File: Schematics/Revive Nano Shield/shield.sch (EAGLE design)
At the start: 24 parts, among them Q3 MOSFET-NCHANNELPTH2

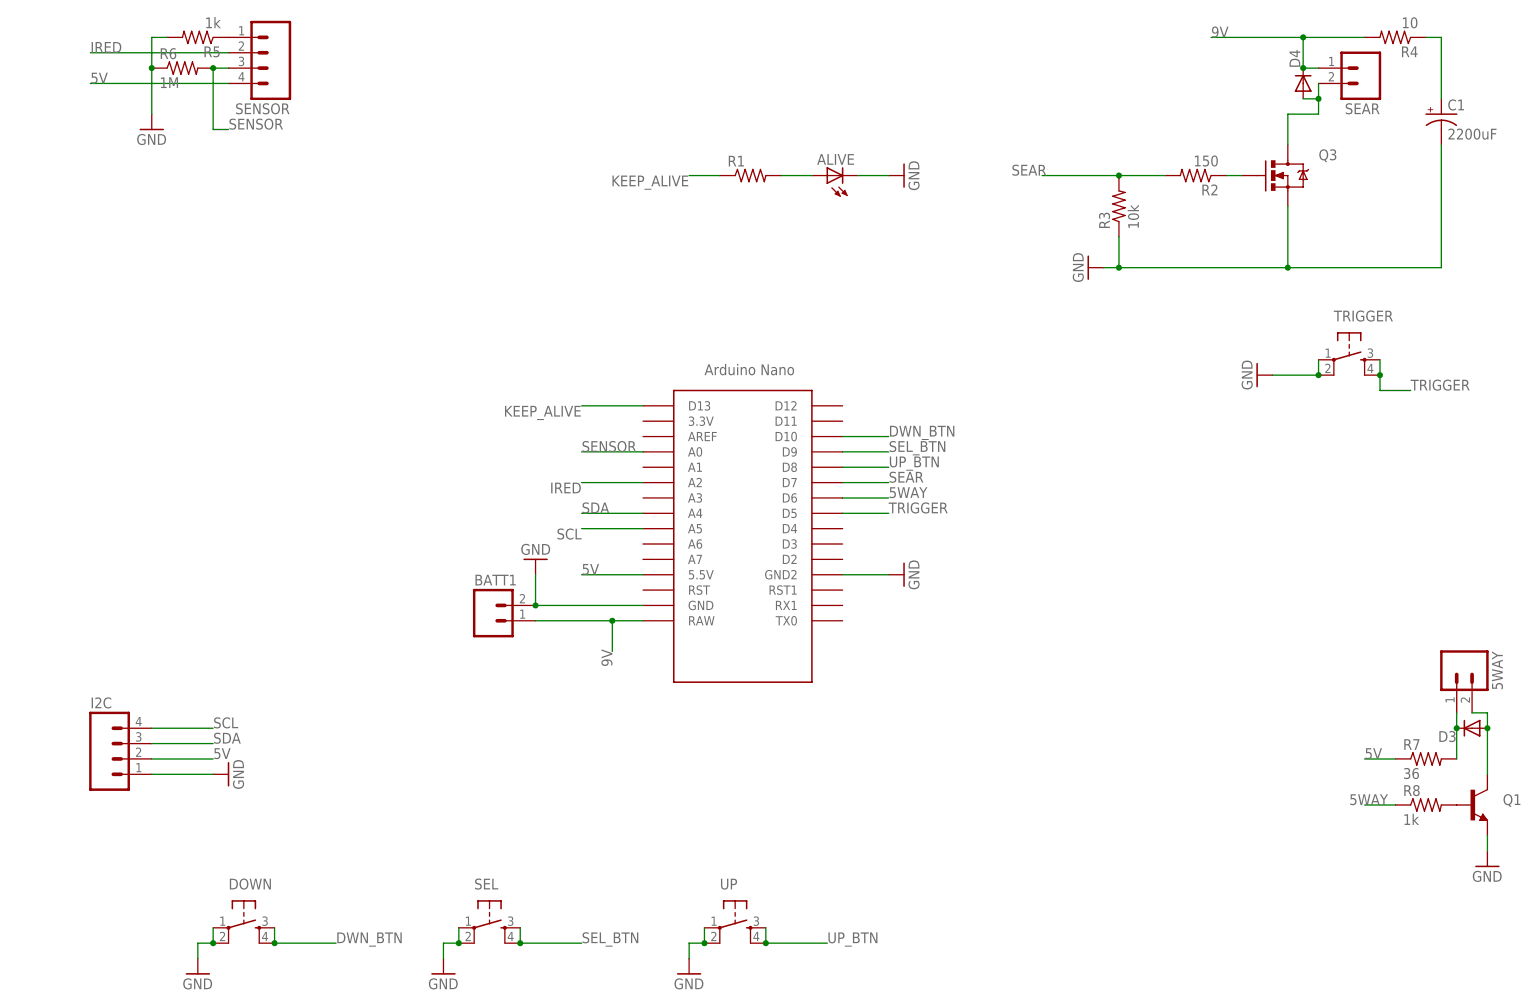
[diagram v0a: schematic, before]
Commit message: Reworks pins to match with new Nano board design
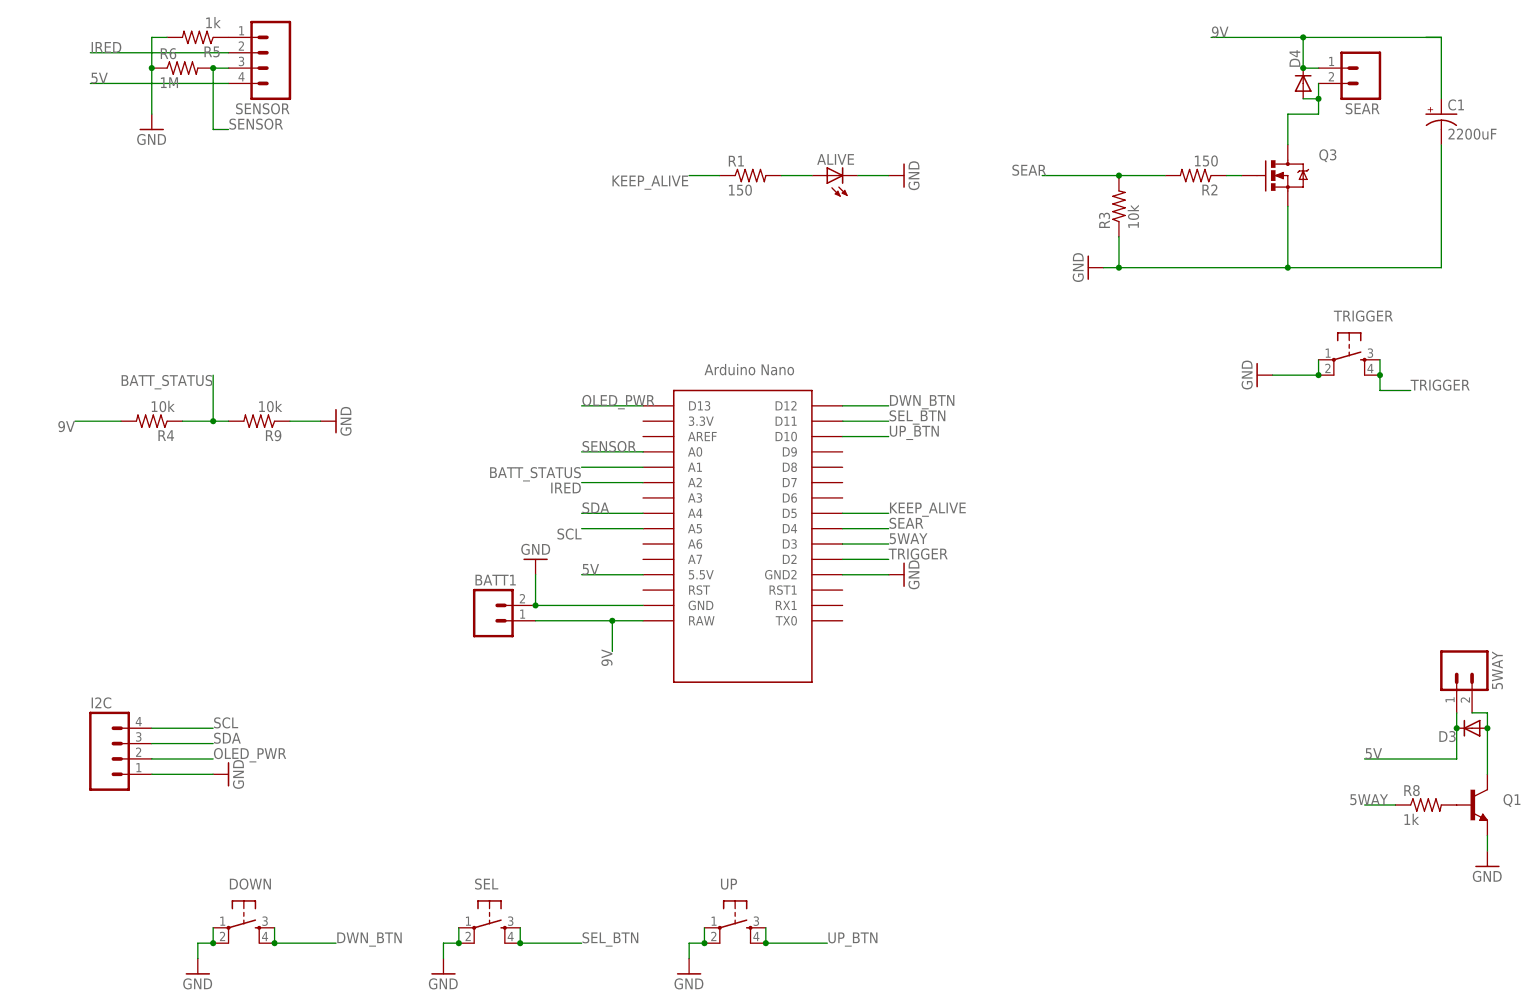
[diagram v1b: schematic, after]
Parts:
- removed R7: 36, SparkFun:RESISTORPTH-1/4W
- added R9: 10k, SparkFun:RESISTORPTH-1/4W
- R1: value (none) -> 150
- R4: value 10 -> 10k
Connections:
- removed net N$4: C1.+, R4.1
- removed net N$5: 5WAY.1, D3.C, R7.2
- new net BATT_STATUS: R4.1, R9.2, U$5.A1
- new net OLED_PWR: I2C.2, U$5.D13
- net 5V: now also 5WAY.1, D3.C; no longer I2C.2, R7.1
- net 5WAY: now also U$5.D3; no longer U$5.D6
- net 9V: now also C1.+
- net DWN_BTN: now also U$5.D12; no longer U$5.D10
- net GND: now also R9.1
- net KEEP_ALIVE: now also U$5.D5; no longer U$5.D13
- net SEAR: now also U$5.D4; no longer U$5.D7
- net SEL_BTN: now also U$5.D11; no longer U$5.D9
- net TRIGGER: now also U$5.D2; no longer U$5.D5
- net UP_BTN: now also U$5.D10; no longer U$5.D8
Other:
- moved on the sheet: R4
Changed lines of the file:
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@@
 <part name="Q3" library="SparkFun" deviceset="MOSFET-NCHANNEL" device="PTH2" value=""/>
 <part name="ALIVE" library="SparkFun" deviceset="LED" device="3MM"/>
-<part name="R1" library="SparkFun" deviceset="RESISTOR" device="PTH-1/4W"/>
+<part name="R1" library="SparkFun" deviceset="RESISTOR" device="PTH-1/4W" value="150"/>
 <part name="GND2" library="SparkFun" deviceset="GND" device=""/>
 <part name="R2" library="SparkFun" deviceset="RESISTOR" device="PTH-1/4W" value="150"/>
-<part name="R4" library="SparkFun" deviceset="RESISTOR" device="PTH-1/4W" value="10"/>
-<part name="R7" library="SparkFun" deviceset="RESISTOR" device="PTH-1/4W" value="36"/>
 <part name="GND5" library="SparkFun" deviceset="GND" device=""/>
 <part name="SEAR" library="SparkFun" deviceset="M02" device="PTH"/>
@@
 <part name="GND7" library="SparkFun" deviceset="GND" device=""/>
 <part name="BATT1" library="SparkFun" deviceset="M02" device="PTH"/>
+<part name="R4" library="SparkFun" deviceset="RESISTOR" device="PTH-1/4W" value="10k"/>
+<part name="R9" library="SparkFun" deviceset="RESISTOR" device="PTH-1/4W" value="10k"/>
+<part name="GND1" library="SparkFun" deviceset="GND" device=""/>
 </parts>
 <sheets>
@@
 <instance part="GND2" gate="1" x="147.32" y="154.94" rot="R90"/>
 <instance part="R2" gate="G$1" x="195.58" y="154.94" rot="R180"/>
-<instance part="R4" gate="G$1" x="228.6" y="177.8" rot="R180"/>
-<instance part="R7" gate="G$1" x="233.68" y="58.42"/>
 <instance part="GND5" gate="1" x="205.74" y="121.92" rot="R270"/>
 <instance part="SEAR" gate="G$1" x="223.52" y="172.72" rot="R180"/>
@@
 <instance part="GND7" gate="1" x="86.36" y="91.44" rot="R180"/>
 <instance part="BATT1" gate="G$1" x="78.74" y="81.28"/>
+<instance part="R4" gate="G$1" x="22.86" y="114.3" rot="R180"/>
+<instance part="R9" gate="G$1" x="40.64" y="114.3" rot="R180"/>
+<instance part="GND1" gate="1" x="53.34" y="114.3" rot="R90"/>
 </instances>
 <busses>
@@
 <wire x1="213.36" y1="172.72" x2="215.9" y2="172.72" width="0.1524" layer="91"/>
 <wire x1="198.12" y1="177.8" x2="213.36" y2="177.8" width="0.1524" layer="91"/>
-<wire x1="213.36" y1="177.8" x2="223.52" y2="177.8" width="0.1524" layer="91"/>
 <wire x1="213.36" y1="172.72" x2="213.36" y2="177.8" width="0.1524" layer="91"/>
-<junction x="213.36" y="177.8"/>
 <label x="198.12" y="177.8" size="1.778" layer="95"/>
 <pinref part="D4" gate="G$1" pin="C"/>
 <junction x="213.36" y="172.72"/>
-<pinref part="R4" gate="G$1" pin="2"/>
 <pinref part="SEAR" gate="G$1" pin="1"/>
+<pinref part="C1" gate="G$1" pin="+"/>
+<wire x1="236.22" y1="167.64" x2="236.22" y2="177.8" width="0.1524" layer="91"/>
+<wire x1="236.22" y1="177.8" x2="213.36" y2="177.8" width="0.1524" layer="91"/>
+<junction x="213.36" y="177.8"/>
 </segment>
 <segment>
@@
 <wire x1="99.06" y1="81.28" x2="99.06" y2="76.2" width="0.1524" layer="91"/>
 <junction x="99.06" y="81.28"/>
+</segment>
+<segment>
+<pinref part="R4" gate="G$1" pin="2"/>
+<wire x1="17.78" y1="114.3" x2="10.16" y2="114.3" width="0.1524" layer="91"/>
+<label x="10.16" y="114.3" size="1.778" layer="95" rot="R180"/>
 </segment>
 </net>
@@
 <wire x1="86.36" y1="83.82" x2="86.36" y2="88.9" width="0.1524" layer="91"/>
 </segment>
+<segment>
+<pinref part="R9" gate="G$1" pin="1"/>
+<pinref part="GND1" gate="1" pin="GND"/>
+<wire x1="50.8" y1="114.3" x2="45.72" y2="114.3" width="0.1524" layer="91"/>
+</segment>
 </net>
 <net name="5V" class="0">
@@
 </segment>
 <segment>
-<pinref part="I2C" gate="G$1" pin="2"/>
-<wire x1="22.86" y1="58.42" x2="33.02" y2="58.42" width="0.1524" layer="91"/>
-<label x="33.02" y="58.42" size="1.778" layer="95"/>
-</segment>
-<segment>
-<pinref part="R7" gate="G$1" pin="1"/>
-<wire x1="228.6" y1="58.42" x2="223.52" y2="58.42" width="0.1524" layer="91"/>
 <label x="223.52" y="58.42" size="1.778" layer="95"/>
+<pinref part="D3" gate="G$1" pin="C"/>
+<wire x1="238.76" y1="63.5" x2="238.76" y2="66.04" width="0.1524" layer="91"/>
+<pinref part="5WAY" gate="G$1" pin="1"/>
+<wire x1="238.76" y1="63.5" x2="238.76" y2="58.42" width="0.1524" layer="91"/>
+<wire x1="238.76" y1="58.42" x2="223.52" y2="58.42" width="0.1524" layer="91"/>
+<junction x="238.76" y="63.5"/>
 </segment>
 <segment>
@@
 </segment>
 <segment>
-<pinref part="U$5" gate="G$1" pin="D5"/>
-<wire x1="137.16" y1="99.06" x2="144.78" y2="99.06" width="0.1524" layer="91"/>
-<label x="144.78" y="99.06" size="1.778" layer="95"/>
+<pinref part="U$5" gate="G$1" pin="D2"/>
+<wire x1="137.16" y1="91.44" x2="144.78" y2="91.44" width="0.1524" layer="91"/>
+<label x="144.78" y="91.44" size="1.778" layer="95"/>
 </segment>
 </net>
@@
 </segment>
 <segment>
-<pinref part="U$5" gate="G$1" pin="D6"/>
-<wire x1="137.16" y1="101.6" x2="144.78" y2="101.6" width="0.1524" layer="91"/>
-<label x="144.78" y="101.6" size="1.778" layer="95"/>
+<pinref part="U$5" gate="G$1" pin="D3"/>
+<wire x1="137.16" y1="93.98" x2="144.78" y2="93.98" width="0.1524" layer="91"/>
+<label x="144.78" y="93.98" size="1.778" layer="95"/>
 </segment>
 </net>
@@
 </segment>
 <segment>
-<pinref part="U$5" gate="G$1" pin="D7"/>
-<wire x1="137.16" y1="104.14" x2="144.78" y2="104.14" width="0.1524" layer="91"/>
-<label x="144.78" y="104.14" size="1.778" layer="95"/>
+<pinref part="U$5" gate="G$1" pin="D4"/>
+<wire x1="137.16" y1="96.52" x2="144.78" y2="96.52" width="0.1524" layer="91"/>
+<label x="144.78" y="96.52" size="1.778" layer="95"/>
 </segment>
 </net>
@@
 </segment>
 <segment>
-<pinref part="U$5" gate="G$1" pin="D8"/>
-<wire x1="137.16" y1="106.68" x2="144.78" y2="106.68" width="0.1524" layer="91"/>
-<label x="144.78" y="106.68" size="1.778" layer="95"/>
+<pinref part="U$5" gate="G$1" pin="D10"/>
+<wire x1="137.16" y1="111.76" x2="144.78" y2="111.76" width="0.1524" layer="91"/>
+<label x="144.78" y="111.76" size="1.778" layer="95"/>
 </segment>
 </net>
@@
 </segment>
 <segment>
-<pinref part="U$5" gate="G$1" pin="D9"/>
-<wire x1="137.16" y1="109.22" x2="144.78" y2="109.22" width="0.1524" layer="91"/>
-<label x="144.78" y="109.22" size="1.778" layer="95"/>
+<pinref part="U$5" gate="G$1" pin="D11"/>
+<wire x1="137.16" y1="114.3" x2="144.78" y2="114.3" width="0.1524" layer="91"/>
+<label x="144.78" y="114.3" size="1.778" layer="95"/>
 </segment>
 </net>
@@
 </segment>
 <segment>
-<pinref part="U$5" gate="G$1" pin="D10"/>
-<wire x1="137.16" y1="111.76" x2="144.78" y2="111.76" width="0.1524" layer="91"/>
-<label x="144.78" y="111.76" size="1.778" layer="95"/>
+<pinref part="U$5" gate="G$1" pin="D12"/>
+<wire x1="137.16" y1="116.84" x2="144.78" y2="116.84" width="0.1524" layer="91"/>
+<label x="144.78" y="116.84" size="1.778" layer="95"/>
 </segment>
 </net>
@@
 </segment>
 <segment>
-<pinref part="U$5" gate="G$1" pin="D13"/>
-<wire x1="104.14" y1="116.84" x2="93.98" y2="116.84" width="0.1524" layer="91"/>
-<label x="93.98" y="116.84" size="1.778" layer="95" rot="R180"/>
+<pinref part="U$5" gate="G$1" pin="D5"/>
+<wire x1="137.16" y1="99.06" x2="144.78" y2="99.06" width="0.1524" layer="91"/>
+<label x="144.78" y="99.06" size="1.778" layer="95"/>
 </segment>
 </net>
@@
 <net name="N$4" class="0">
 <segment>
-<pinref part="R4" gate="G$1" pin="1"/>
 <wire x1="233.68" y1="177.8" x2="236.22" y2="177.8" width="0.1524" layer="91"/>
-<wire x1="236.22" y1="177.8" x2="236.22" y2="167.64" width="0.1524" layer="91"/>
-<pinref part="C1" gate="G$1" pin="+"/>
-</segment>
-</net>
-<net name="N$5" class="0">
-<segment>
-<pinref part="R7" gate="G$1" pin="2"/>
-<pinref part="D3" gate="G$1" pin="C"/>
-<wire x1="238.76" y1="58.42" x2="238.76" y2="63.5" width="0.1524" layer="91"/>
-<wire x1="238.76" y1="63.5" x2="238.76" y2="66.04" width="0.1524" layer="91"/>
-<junction x="238.76" y="63.5"/>
-<pinref part="5WAY" gate="G$1" pin="1"/>
 </segment>
 </net>
@@
 </segment>
 </net>
+<net name="OLED_PWR" class="0">
+<segment>
+<pinref part="I2C" gate="G$1" pin="2"/>
+<wire x1="22.86" y1="58.42" x2="33.02" y2="58.42" width="0.1524" layer="91"/>
+<label x="33.02" y="58.42" size="1.778" layer="95"/>
+</segment>
+<segment>
+<pinref part="U$5" gate="G$1" pin="D13"/>
+<wire x1="104.14" y1="116.84" x2="93.98" y2="116.84" width="0.1524" layer="91"/>
+<label x="93.98" y="116.84" size="1.778" layer="95"/>
+</segment>
+</net>
+<net name="BATT_STATUS" class="0">
+<segment>
+<pinref part="R4" gate="G$1" pin="1"/>
+<pinref part="R9" gate="G$1" pin="2"/>
+<wire x1="35.56" y1="114.3" x2="33.02" y2="114.3" width="0.1524" layer="91"/>
+<wire x1="33.02" y1="114.3" x2="27.94" y2="114.3" width="0.1524" layer="91"/>
+<wire x1="33.02" y1="114.3" x2="33.02" y2="121.92" width="0.1524" layer="91"/>
+<junction x="33.02" y="114.3"/>
+<label x="33.02" y="121.92" size="1.778" layer="95" rot="R180"/>
+</segment>
+<segment>
+<pinref part="U$5" gate="G$1" pin="A1"/>
+<wire x1="104.14" y1="106.68" x2="93.98" y2="106.68" width="0.1524" layer="91"/>
+<label x="93.98" y="106.68" size="1.778" layer="95" rot="R180"/>
+</segment>
+</net>

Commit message: Updated schematics
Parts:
- removed SENSOR: (no value), SparkFun:M04PTH
- added A/C_EYE: (no value), SparkFun:M04PTH
- added SLG_EYE: (no value), SparkFun-Connectors:CONN_03
- added SPI: (no value), SparkFun-Connectors:CONN_07
- R4, R5, R6, R9: device SparkFun:RESISTORPTH-1/4W -> resistor:R-EU_0309/V
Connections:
- net SCL renamed I2C_CLK
- net SDA renamed I2C_SDA
- removed net IRED: SENSOR.2, U$5.A2
- removed net N$6: R5.1, SENSOR.1
- removed net SENSOR: R6.2, SENSOR.3, U$5.A0
- new net EYE_GND: A/C_EYE.1, R5.1
- new net EYE_PWR: A/C_EYE.2, SLG_EYE.2, U$5.A2
- new net EYE_READ: A/C_EYE.3, R6.2, SLG_EYE.1, U$5.A0
- new net N$12: U$5.TX0
- new net N$13: U$5.RX1
- new net SPI_CLK: SPI.3, U$5.D13
- new net SPI_CS: SPI.7, U$5.D9
- new net SPI_DC: SPI.6, U$5.D10
- new net SPI_MOSI: SPI.5, U$5.D11
- new net SPI_RES: SPI.4, U$5.D12
- net 5V: now also A/C_EYE.4, SPI.2; no longer SENSOR.4
- net DWN_BTN: now also U$5.D8; no longer U$5.D12
- net GND: now also SLG_EYE.3, SPI.1
- net OLED_PWR: now also U$5.A3; no longer U$5.D13
- net SEL_BTN: now also U$5.D7; no longer U$5.D11
- net UP_BTN: now also U$5.D6; no longer U$5.D10
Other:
- note added: "Red"
- note added: "SLG_RED is backwards used as sensor"
- moved on the sheet: BATT1

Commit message: Tweaked board layout to fit everything nicer
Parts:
- removed R4: 10k, resistor:R-EU_0309/V
- added R7: 10k, SparkFun:RESISTORPTH-1/4W
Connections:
- removed net SPI_CS: SPI.7, U$5.D9
- net 9V: now also R7.1; no longer R4.2
- net BATT_STATUS: now also R7.2; no longer R4.1
- net GND: now also SPI.7
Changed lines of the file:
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@@
 <part name="GND7" library="SparkFun" deviceset="GND" device=""/>
 <part name="BATT1" library="SparkFun" deviceset="M02" device="PTH"/>
-<part name="R4" library="resistor" library_urn="urn:adsk.eagle:library:348" deviceset="R-EU_" device="0309/V" package3d_urn="urn:adsk.eagle:package:26090/1" value="10k"/>
 <part name="R9" library="resistor" library_urn="urn:adsk.eagle:library:348" deviceset="R-EU_" device="0309/V" package3d_urn="urn:adsk.eagle:package:26090/1" value="10k"/>
 <part name="GND1" library="SparkFun" deviceset="GND" device=""/>
@@
 <part name="SPI" library="SparkFun-Connectors" library_urn="urn:adsk.eagle:library:513" deviceset="CONN_07" device="" package3d_urn="urn:adsk.eagle:package:38129/1"/>
 <part name="GND8" library="SparkFun" deviceset="GND" device=""/>
+<part name="GND9" library="SparkFun" deviceset="GND" device=""/>
+<part name="R7" library="SparkFun" deviceset="RESISTOR" device="PTH-1/4W" value="10k"/>
 </parts>
 <sheets>
@@
 <instance part="GND7" gate="1" x="76.2" y="91.44" rot="R180"/>
 <instance part="BATT1" gate="G$1" x="68.58" y="81.28"/>
-<instance part="R4" gate="G$1" x="22.86" y="114.3" rot="R180"/>
 <instance part="R9" gate="G$1" x="40.64" y="114.3" rot="R180"/>
 <instance part="GND1" gate="1" x="53.34" y="114.3" rot="R90"/>
@@
 <instance part="SPI" gate="G$1" x="17.78" y="83.82"/>
 <instance part="GND8" gate="1" x="33.02" y="76.2"/>
+<instance part="GND9" gate="1" x="30.48" y="96.52" rot="R180"/>
+<instance part="R7" gate="G$1" x="22.86" y="114.3"/>
 </instances>
 <busses>
@@
 </segment>
 <segment>
-<pinref part="R4" gate="G$1" pin="2"/>
 <wire x1="17.78" y1="114.3" x2="10.16" y2="114.3" width="0.1524" layer="91"/>
 <label x="10.16" y="114.3" size="1.778" layer="95" rot="R180"/>
+<pinref part="R7" gate="G$1" pin="1"/>
 </segment>
 </net>
@@
 <pinref part="GND8" gate="1" pin="GND"/>
 </segment>
+<segment>
+<pinref part="SPI" gate="G$1" pin="7"/>
+<wire x1="22.86" y1="93.98" x2="30.48" y2="93.98" width="0.1524" layer="91"/>
+<label x="33.02" y="93.98" size="1.778" layer="95"/>
+<pinref part="GND9" gate="1" pin="GND"/>
+<wire x1="30.48" y1="93.98" x2="33.02" y2="93.98" width="0.1524" layer="91"/>
+<junction x="30.48" y="93.98"/>
+</segment>
 </net>
 <net name="5V" class="0">
@@
 <net name="BATT_STATUS" class="0">
 <segment>
-<pinref part="R4" gate="G$1" pin="1"/>
 <pinref part="R9" gate="G$1" pin="2"/>
 <wire x1="35.56" y1="114.3" x2="33.02" y2="114.3" width="0.1524" layer="91"/>
@@
 <junction x="33.02" y="114.3"/>
 <label x="33.02" y="121.92" size="1.778" layer="95" rot="R180"/>
+<pinref part="R7" gate="G$1" pin="2"/>
 </segment>
 <segment>
@@
 </segment>
 </net>
-<net name="SPI_CS" class="0">
-<segment>
-<pinref part="U$5" gate="G$1" pin="D9"/>
-<wire x1="137.16" y1="109.22" x2="144.78" y2="109.22" width="0.1524" layer="91"/>
-<label x="144.78" y="109.22" size="1.778" layer="95"/>
-</segment>
-<segment>
-<pinref part="SPI" gate="G$1" pin="7"/>
-<wire x1="22.86" y1="93.98" x2="33.02" y2="93.98" width="0.1524" layer="91"/>
-<label x="33.02" y="93.98" size="1.778" layer="95"/>
-</segment>
-</net>
